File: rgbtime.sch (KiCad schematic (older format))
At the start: 41 parts, among them CON1 AVR-ISP-6, IC1 ATMEGA8-AI, IC10 WS2812B, IC11 WS2812B, IC12 WS2812B, IC13 WS2812B, IC14 WS2812B, IC15 WS2812B, IC16 WS2812B, IC17 WS2812B, IC18 WS2812B, IC19 WS2812B, IC2 WS2812B, IC20 WS2812B, IC21 WS2812B, IC22 WS2812B, IC23 WS2812B, IC24 WS2812B, IC25 WS2812B, IC26 WS2812B, IC3 WS2812B, IC4 WS2812B, IC5 WS2812B, IC6 WS2812B, IC7 WS2812B, IC8 WS2812B, IC9 WS2812B, P1 USB-Mini-B, U1 MCP79410, U2 LM75, Y1 CC4V-T1A-32768

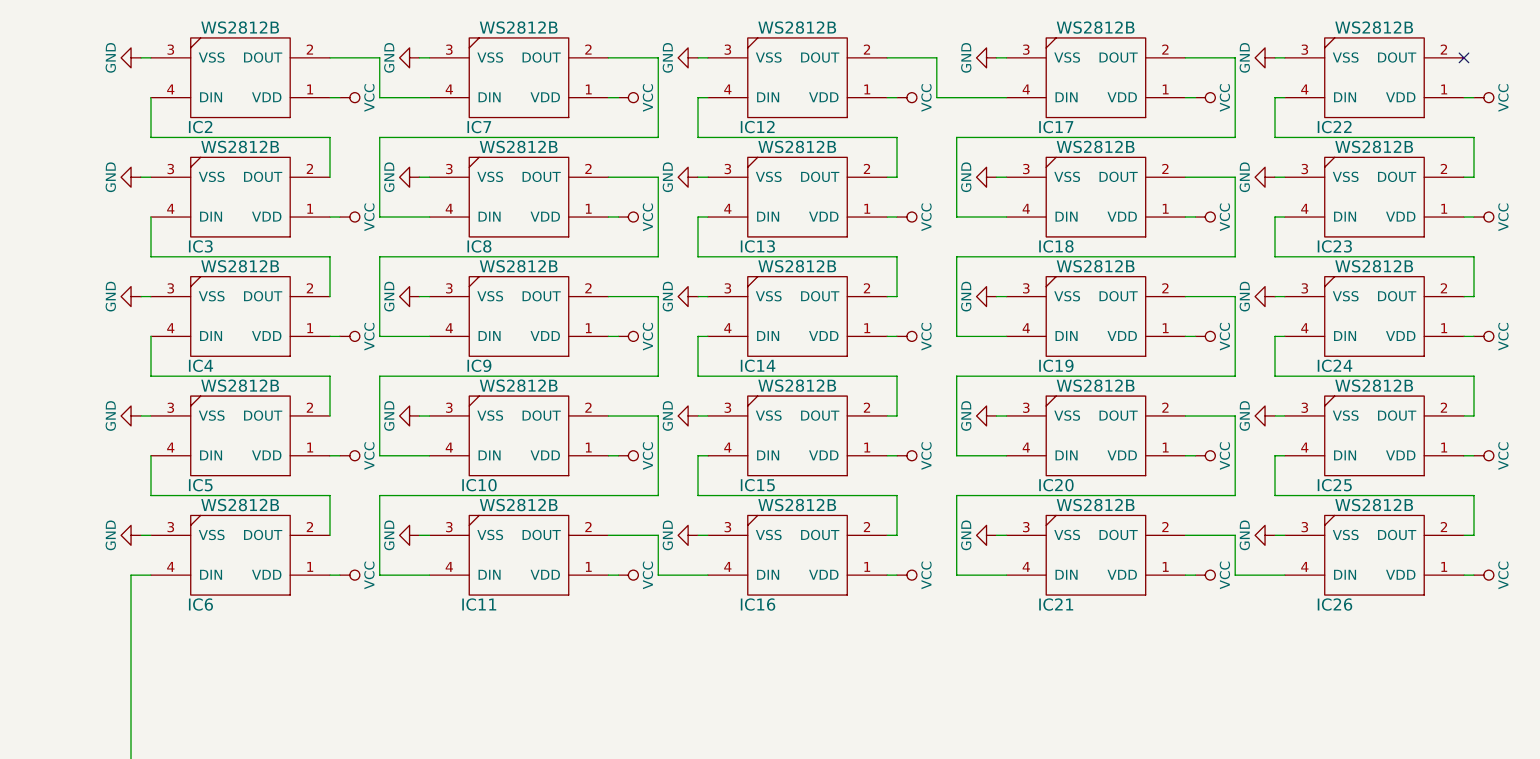
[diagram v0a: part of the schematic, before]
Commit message: started layout, matrix placed, need USB footprint
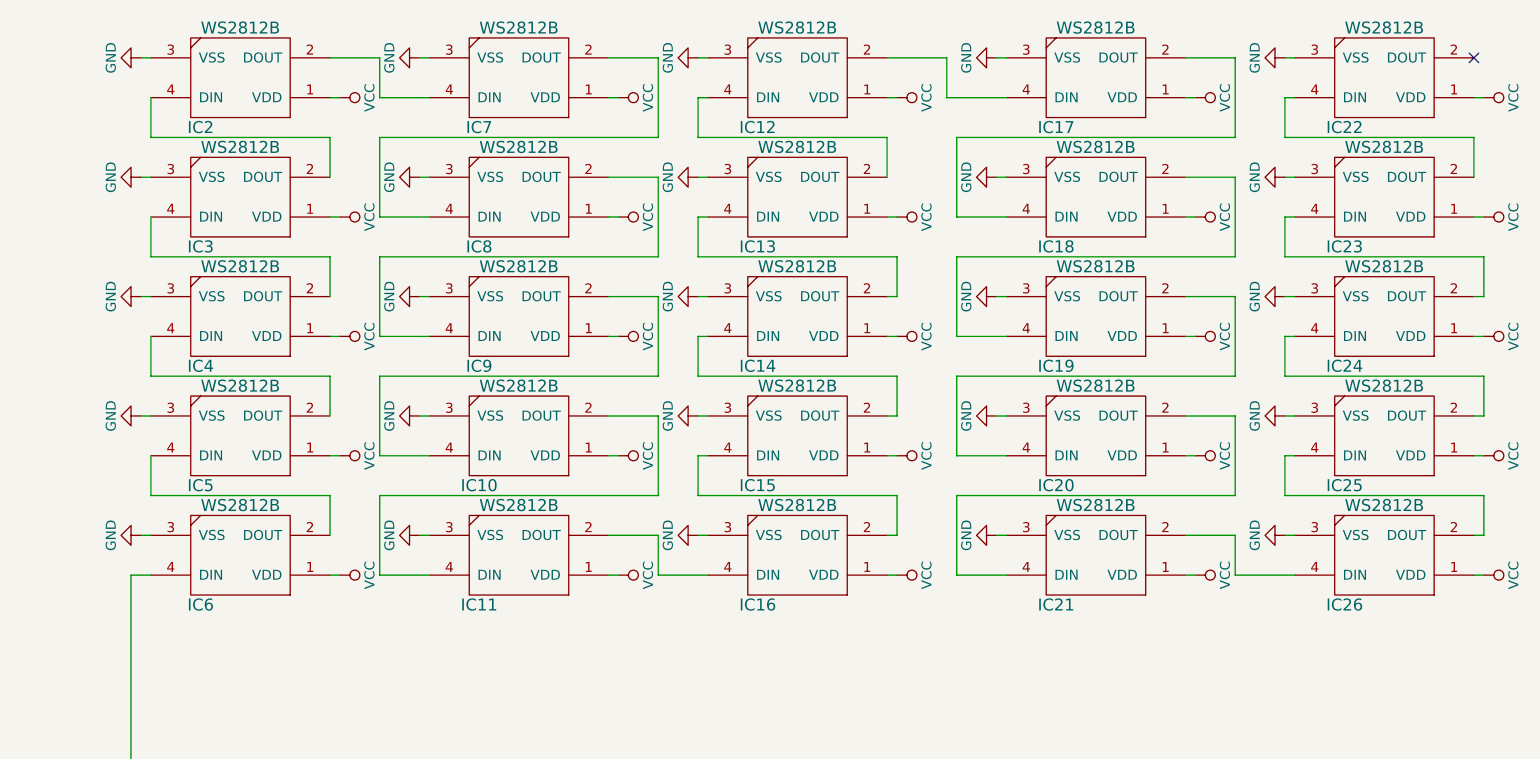
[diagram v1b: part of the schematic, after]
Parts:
- removed IC24, IC25: WS2812B, devthrash:WS2812B, symbol WS2812B
- added IC12, IC13: WS2812B, devthrash:WS2812B, symbol WS2812B
- renumbered IC12 to IC24, IC13 to IC25
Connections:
- net GND: now also IC12.3 (VSS), IC13.3 (VSS)
- net VCC: now also IC12.1 (VDD), IC13.1 (VDD)
- net at IC14.2 (DOUT): now also IC13.4 (DIN); no longer IC25.4 (DIN)
- net at IC17.4 (DIN): now also IC12.2 (DOUT); no longer IC24.2 (DOUT)
- net at IC26.2 (DOUT): now also IC25.4 (DIN)
- net at IC23.4 (DIN): now also IC24.2 (DOUT)
- new net: IC12.4 (DIN), IC13.2 (DOUT)
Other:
- moved on the sheet: IC24, IC25
